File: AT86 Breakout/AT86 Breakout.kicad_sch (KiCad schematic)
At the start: 19 parts, among them J1 Conn_01x04, J2 Conn_01x04, J3 Conn_01x07, J5 Conn_01x10, U1 AT86RF215-ZU

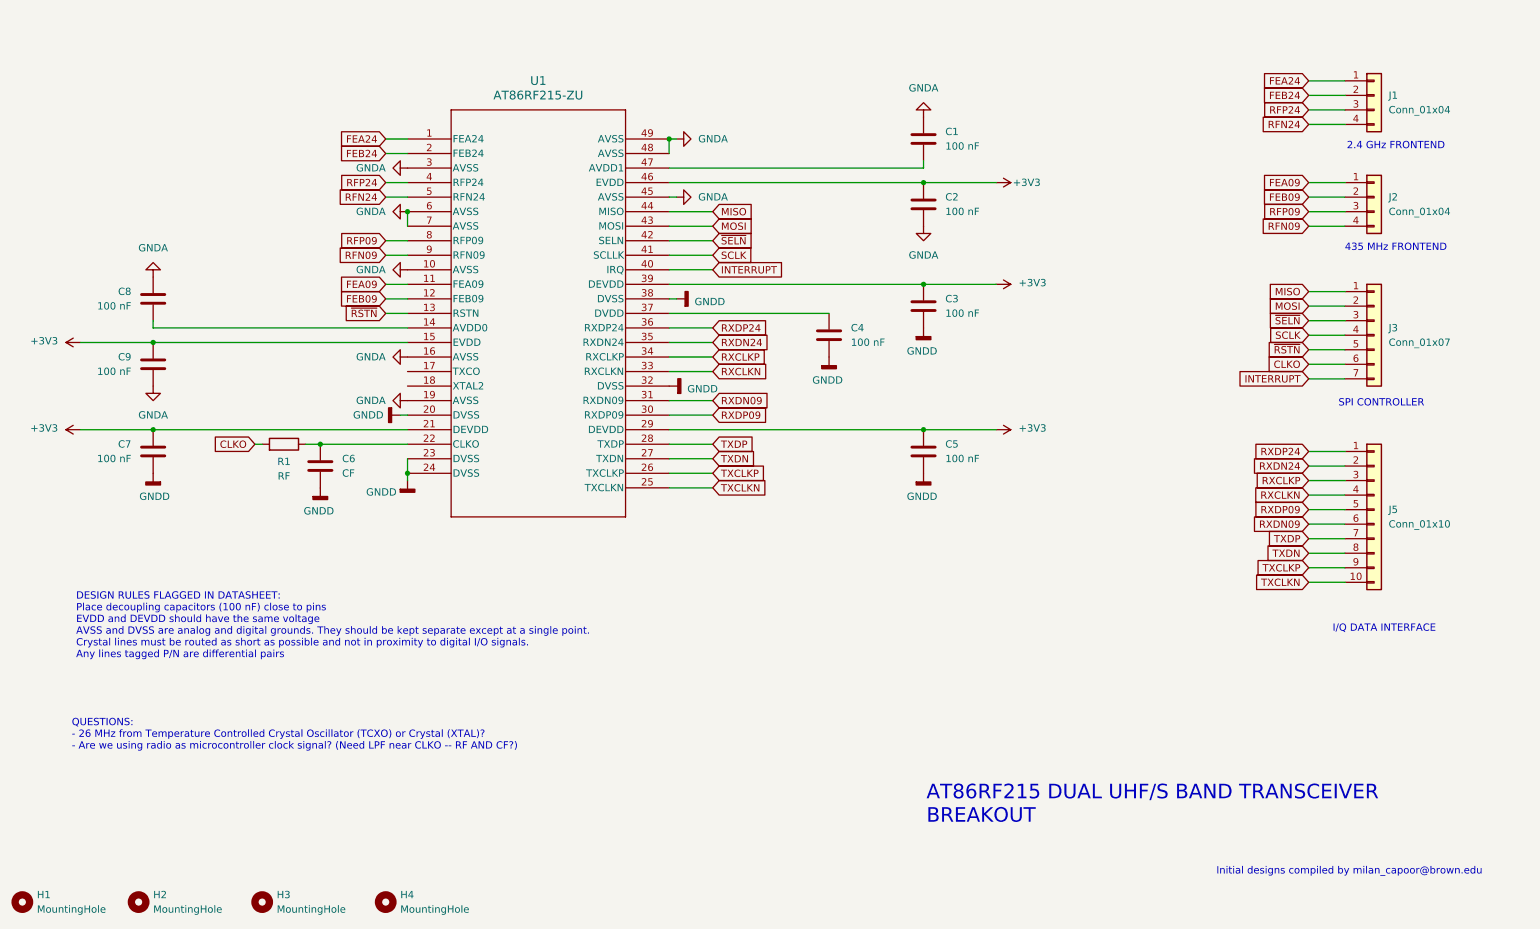
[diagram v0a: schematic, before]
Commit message: initial frontend layout
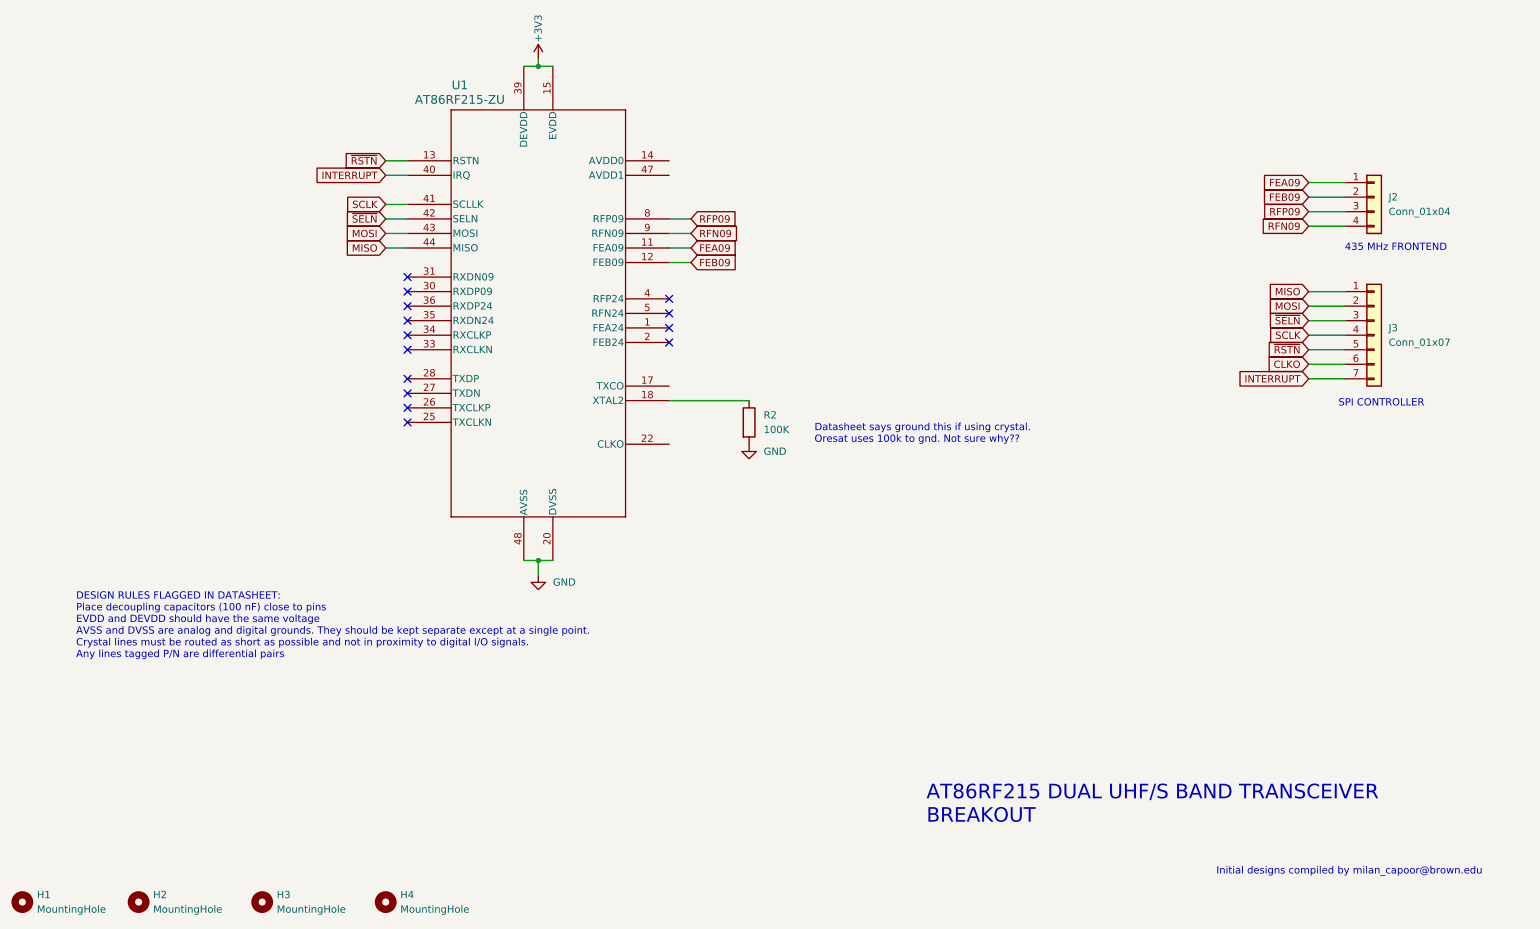
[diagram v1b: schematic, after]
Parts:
- removed C1, C2, C3, C4, C5, C7, C8, C9: 100 nF, symbol Device:C
- removed C6: CF, symbol Device:C
- removed J1: Conn_01x04, symbol Connector_Generic:Conn_01x04
- removed J5: Conn_01x10, symbol Connector_Generic:Conn_01x10
- removed R1: RF, symbol Device:R
- added R2: 100K, symbol Device:R
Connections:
- net +3V3: no longer U1.21 (DEVDD), U1.29 (DEVDD), U1.46 (EVDD)
- net at U1.18 (XTAL2): now also R2.1
- net FEA24: no longer names the net of U1.1 (FEA24)
- net FEB24: no longer names the net of U1.2 (FEB24)
- removed net GNDA: U1.10 (AVSS), U1.16 (AVSS), U1.19 (AVSS), U1.3 (AVSS), U1.45 (AVSS), U1.48 (AVSS), U1.49 (AVSS), U1.6 (AVSS), U1.7 (AVSS)
- removed net GNDD: U1.20 (DVSS), U1.23 (DVSS), U1.24 (DVSS), U1.32 (DVSS), U1.38 (DVSS)
- net RFN24: no longer names the net of U1.5 (RFN24)
- net RFP24: no longer names the net of U1.4 (RFP24)
- net RXCLKN: no longer names the net of U1.33 (RXCLKN)
- net RXCLKP: no longer names the net of U1.34 (RXCLKP)
- net RXDN09: no longer names the net of U1.31 (RXDN09)
- net RXDN24: no longer names the net of U1.35 (RXDN24)
- net RXDP09: no longer names the net of U1.30 (RXDP09)
- net RXDP24: no longer names the net of U1.36 (RXDP24)
- net TXCLKN: no longer names the net of U1.25 (TXCLKN)
- net TXCLKP: no longer names the net of U1.26 (TXCLKP)
- net TXDN: no longer names the net of U1.27 (TXDN)
- net TXDP: no longer names the net of U1.28 (TXDP)
- new net GND: R2.2, U1.20 (DVSS), U1.48 (AVSS)
- no-connect marks 0 -> 14
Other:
- note added: "Datasheet says ground this if using crystal. Oresat uses 100k to gnd. Not sure why??"
- note removed: "2.4 GHz FRONTEND"
- note removed: "I/Q DATA INTERFACE"
- note removed: "QUESTIONS: - 26 MHz from Temperature Controlled Crystal Oscillator (TCXO) or Crystal (XTAL)? - Are we using radio as microcontroller clock signal? (Need LPF near CLKO -- RF AND CF?)"
